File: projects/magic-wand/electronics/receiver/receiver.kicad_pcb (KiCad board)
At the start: 4 copper layers, 50 x 42 mm, 46 parts, among them J1 USB-C-16P, J2 DF13A-5P-1.25H(51), J3 ISO_OC_2P, J4 LOAD_OUT_3P, Q1 CSD17313Q2, U1 NINA-B302-00B-00, U2 TPS62162DSGR, U3 SN74LVC2T45DCUR, U4 SN74LVC2T45DCUR, U5 TLP291(SE), U6 USBLC6-2SC6

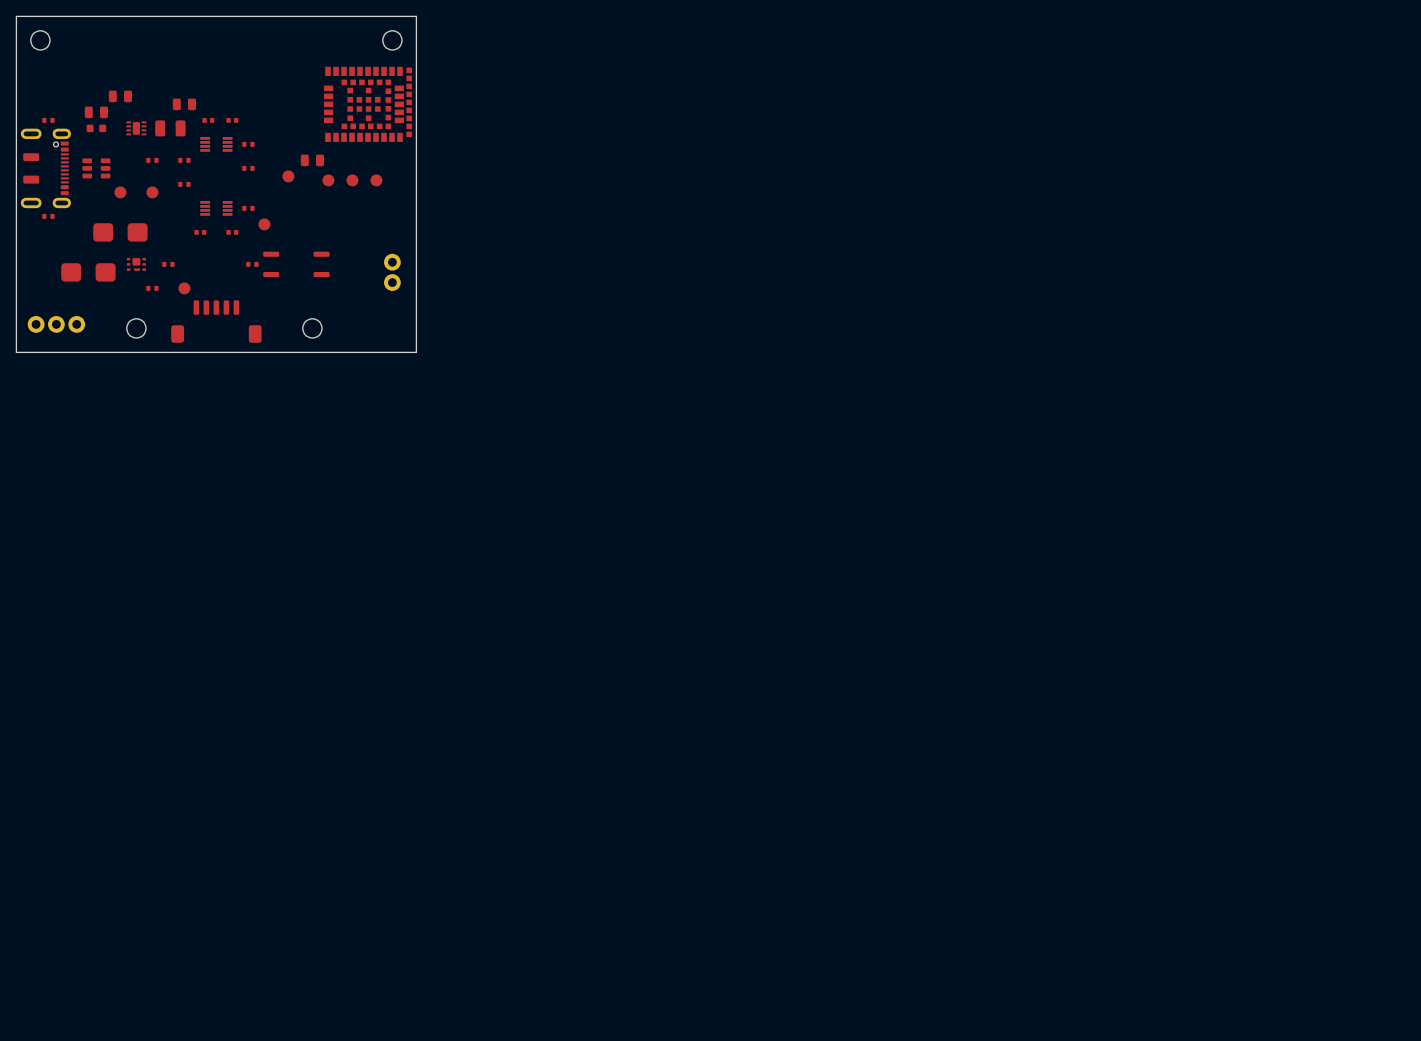
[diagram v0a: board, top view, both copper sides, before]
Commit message: fix: center generated KiCad boards on A4 worksheet
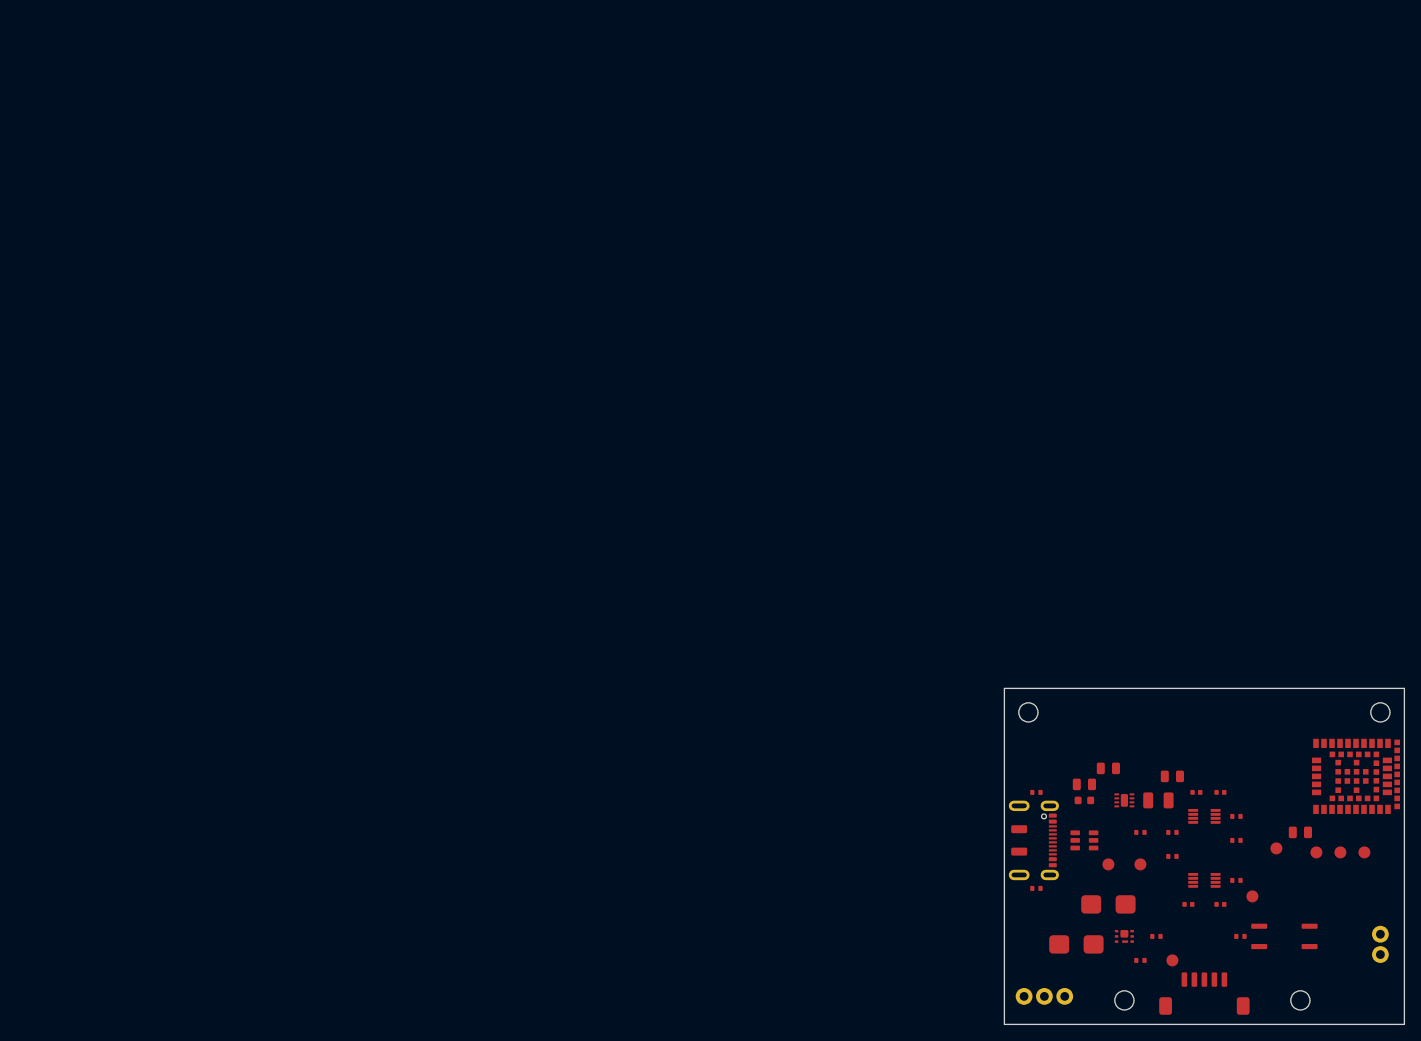
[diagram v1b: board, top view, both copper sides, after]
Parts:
- moved C_BUCK_IN 149.4 mm to (136.5, 94.0)
- moved C_BUCK_OUT 149.4 mm to (144.5, 95.0)
- moved C_U1 149.4 mm to (160.5, 102.0)
- moved C_U3A 149.4 mm to (147.5, 97.0)
- moved C_U3B 149.4 mm to (150.5, 97.0)
- moved C_U4A 149.4 mm to (146.5, 111.0)
- moved C_U4B 149.4 mm to (150.5, 111.0)
- moved C_USB 149.4 mm to (133.5, 96.0)
- moved D1 149.4 mm to (132.5, 116.0)
- moved D2 149.4 mm to (136.5, 111.0)
- moved F1 149.4 mm to (133.5, 98.0)
- moved H1 149.4 mm to (126.5, 87.0)
- moved H2 149.4 mm to (170.5, 87.0)
- moved H3 149.4 mm to (138.5, 123.0)
- moved H4 149.4 mm to (160.5, 123.0)
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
